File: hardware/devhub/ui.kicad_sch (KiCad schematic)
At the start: 12 parts, among them U10 74HC595, U11 74HC595

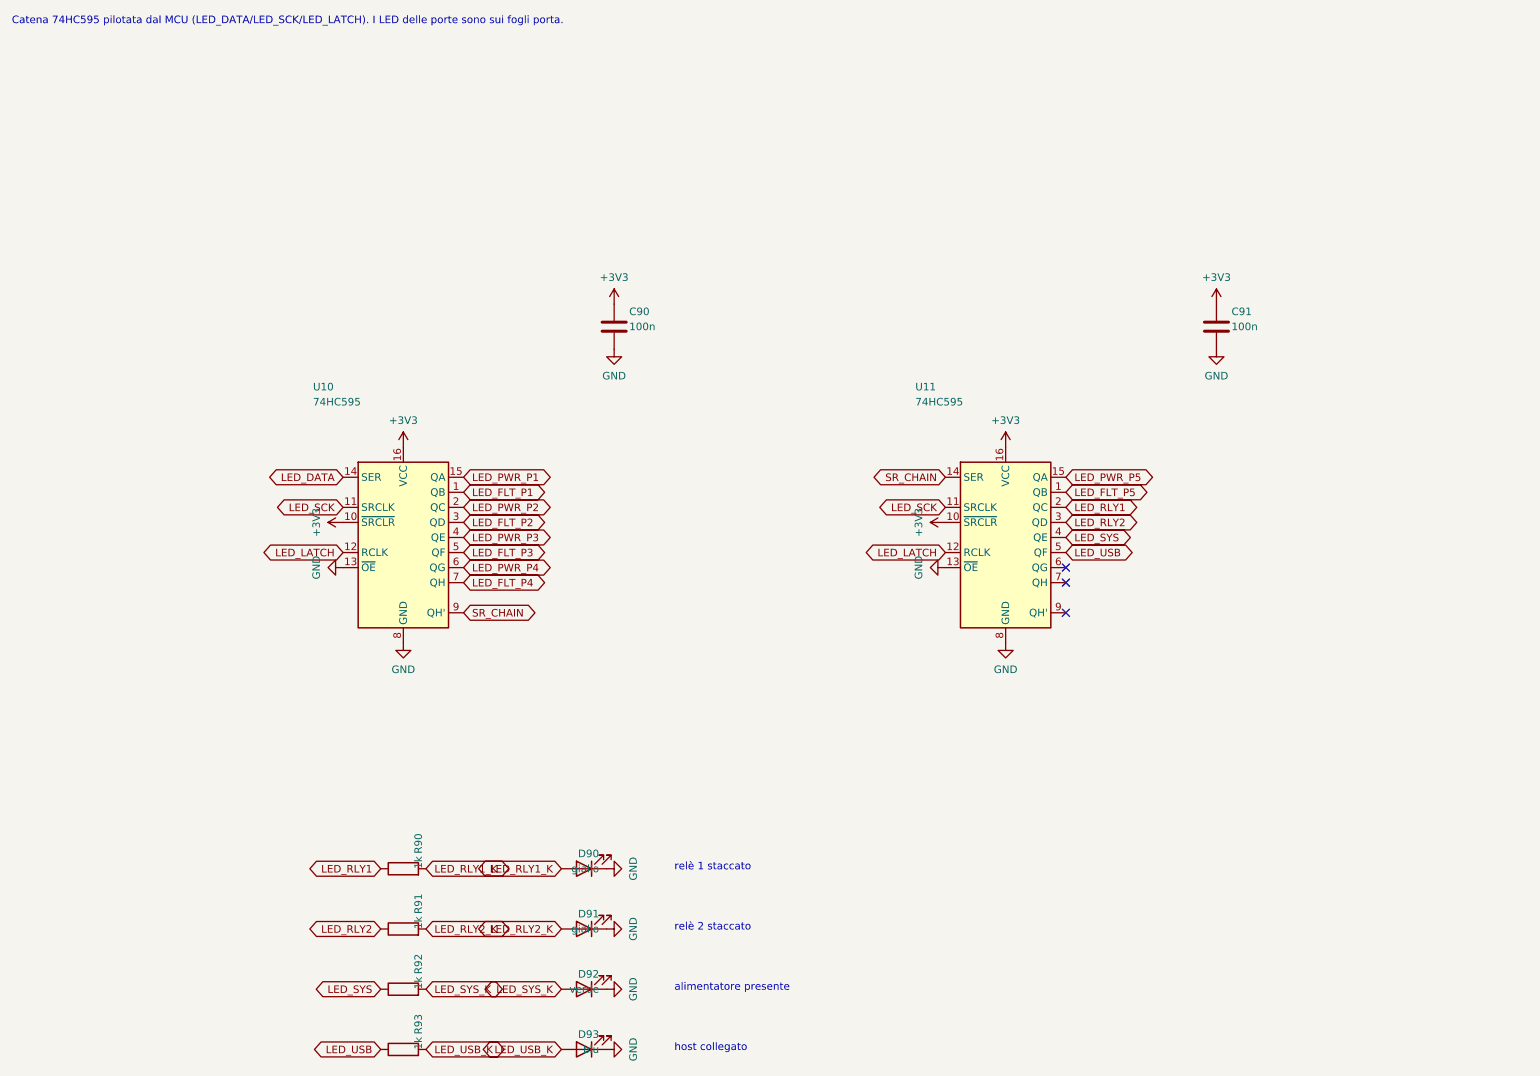
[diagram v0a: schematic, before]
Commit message: Schematic v0.2: hub reset supervisor, 1 A LDO, reorganized sheets, USB connectors and crystal
Functional changes:
- USB2517 RESET_N with pull-up and MCP120T-300 supervisor, wired-OR with
  the MCU (open-drain): resetting the MCU no longer resets the hub, so the
  ST DFU bootloader is reachable through it (D16/D17).
- 3.3 V LDO: AP7361C-33E (1 A, SOT-223) instead of AP2112K, which
  dissipated too much with the hub load.
- 74HC595 /OE on PB6 with pull-up: LEDs off until firmware enables them.
- Orange D93 instead of blue, USB-A bulk capacitance >= 120 uF, relay coil
  pinout fixed, snubbers marked DNP, Cliff FCR7350 banana jack footprints.
- D18: horizontal USB connectors, GCT USB4105-GF-A (USB-C) and Kycon
  KUSBX-AS1N-B (USB-A).
- D19: YXC X322524MOB4SI 24 MHz crystal (C_L 12 pF), 15 pF C0G load caps.

Layout: nearby parts wired directly, every net still explicitly named;
local labels inside sheets, global only across sheets, hierarchical for
ports. Files saved with KiCad 10.

Connectivity checked against the previous netlist, ERC clean.
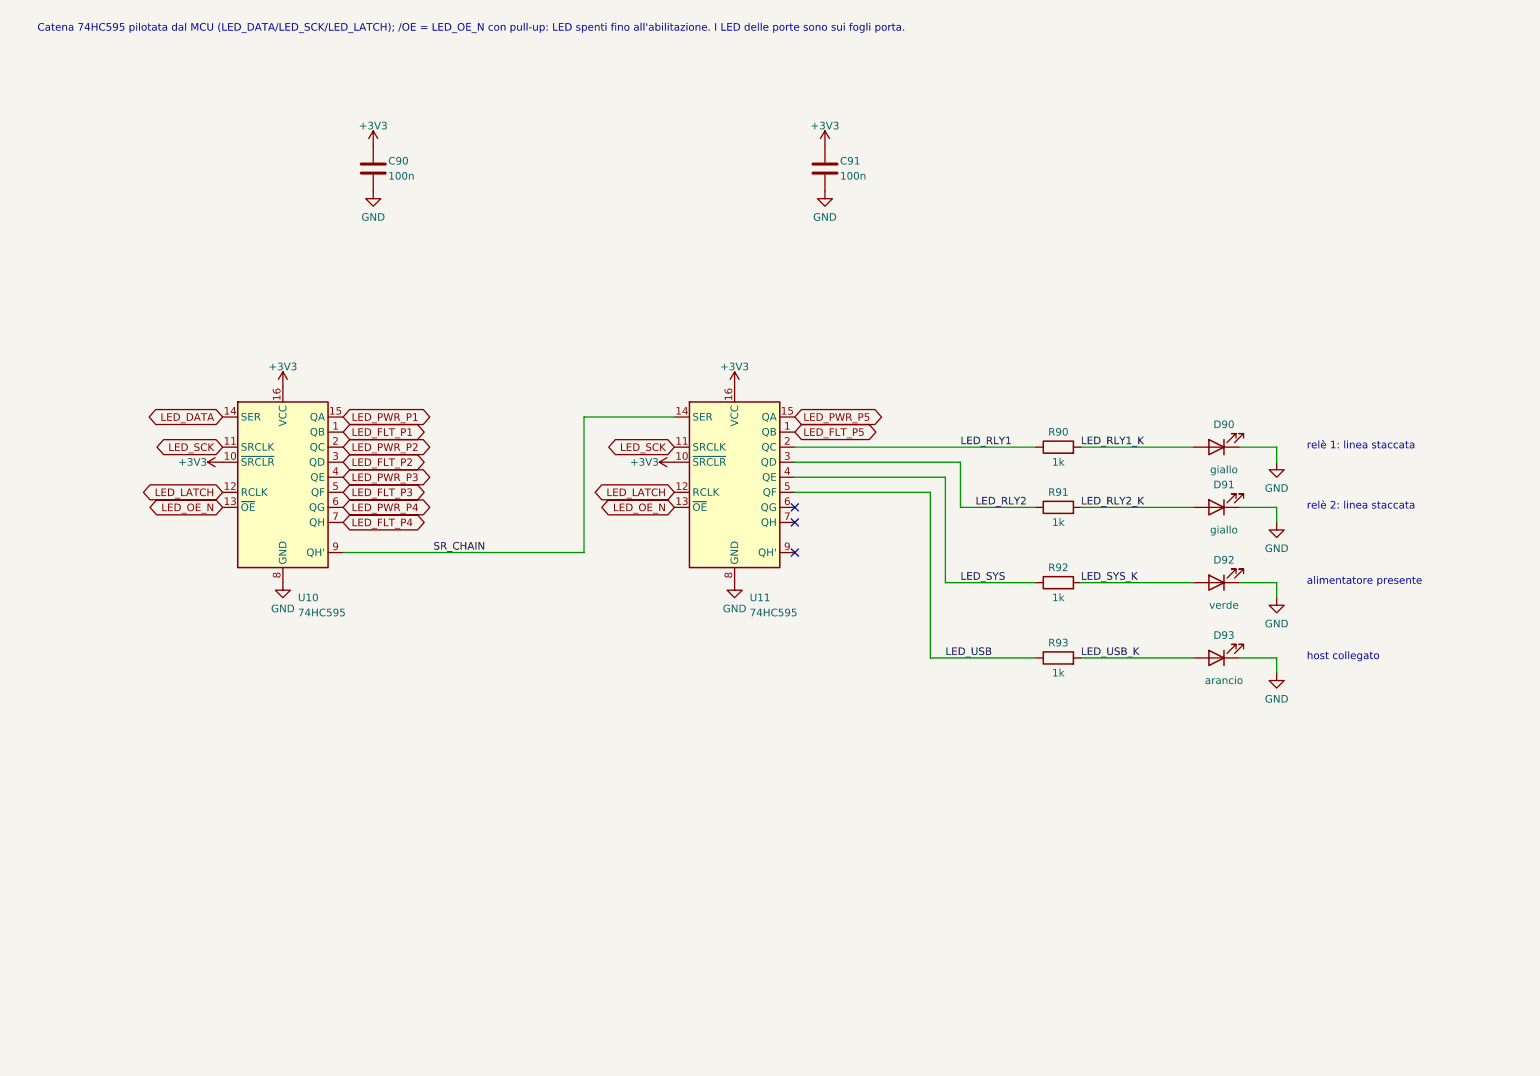
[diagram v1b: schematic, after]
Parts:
- D93: value blu -> arancio
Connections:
- net GND: no longer U10.13 (~{OE}), U11.13 (~{OE})
- new net LED_OE_N: U10.13 (~{OE}), U11.13 (~{OE})
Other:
- note added: "Catena 74HC595 pilotata dal MCU (LED_DATA/LED_SCK/LED_LATCH); /OE = LED_OE_N con pull-up: LED spenti fino all'abilitazione. I LED delle porte sono sui fogli porta."
- note added: "relè 1: linea staccata"
- note added: "relè 2: linea staccata"
- note removed: "Catena 74HC595 pilotata dal MCU (LED_DATA/LED_SCK/LED_LATCH). I LED delle porte sono sui fogli porta."
- note removed: "relè 1 staccato"
- note removed: "relè 2 staccato"

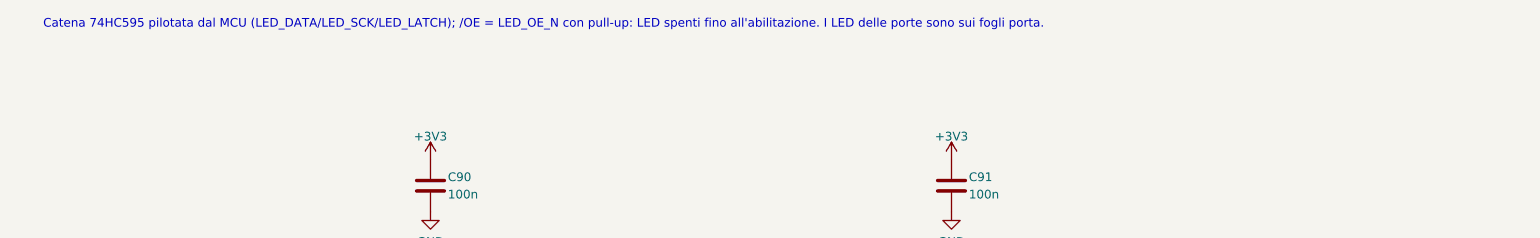
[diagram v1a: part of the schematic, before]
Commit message: Lab-use protection: TPS259470A input eFuse, PI3USB4002A data switches; AGENTS.md
Power input (D20, D21):
- TPS259470A eFuse after the shunt: trips above 5.84 V and below 4.0 V,
  zener on EN to withstand up to 28 V, 3.5 A limit, ~5 ms soft start,
  auto-retry, FLT to the MCU on PB1.
- The shunt stays before the eFuse, so the INA3221 still measures the input
  voltage when the eFuse is off.

Ports (D22): PI3USB4002A instead of TS3USB30E. The connector side withstands
24 V and opens above 4.75 V, so a D+/D- short to VBUS on a board under test
no longer reaches the 3.3 V rail.

Symbols for both ICs added to the project library. AGENTS.md added: the
schematic is edited in KiCad or with targeted changes, never regenerated by
script. Sheets re-saved by KiCad.

Connectivity checked against the previous netlist, ERC clean.
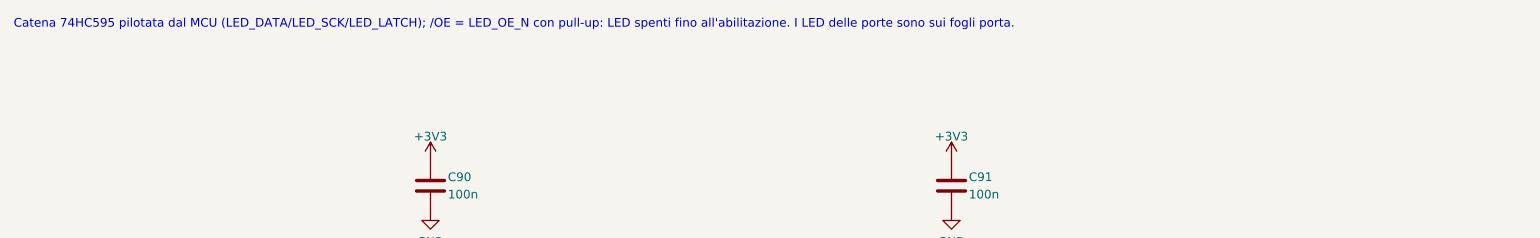
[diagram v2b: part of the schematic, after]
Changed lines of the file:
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@@
 	(text "Catena 74HC595 pilotata dal MCU (LED_DATA/LED_SCK/LED_LATCH); /OE = LED_OE_N con pull-up: LED spenti fino all'abilitazione. I LED delle porte sono sui fogli porta."
 		(exclude_from_sim no)
-		(at 14.478 16.51 0)
+		(at 10.16 16.51 0)
 		(effects
 			(font
@@
 		(in_pos_files yes)
 		(dnp no)
-		(property "Reference" "#PWR138"
+		(property "Reference" "#PWR145"
 			(at 71.12 35.56 0)
 			(hide yes)
@@
 			(project "devhub"
 				(path "/af6ea7d8-d1ba-5fc6-aec8-abf514847630/c82dde94-3a77-5cb6-9c61-f280daabce7c"
-					(reference "#PWR138")
+					(reference "#PWR145")
 					(unit 1)
 				)
@@
 		(in_pos_files yes)
 		(dnp no)
-		(property "Reference" "#PWR137"
+		(property "Reference" "#PWR144"
 			(at 132.08 76.2 0)
 			(hide yes)
@@
 			(project "devhub"
 				(path "/af6ea7d8-d1ba-5fc6-aec8-abf514847630/c82dde94-3a77-5cb6-9c61-f280daabce7c"
-					(reference "#PWR137")
+					(reference "#PWR144")
 					(unit 1)
 				)
@@
 		(in_pos_files yes)
 		(dnp no)
-		(property "Reference" "#PWR140"
+		(property "Reference" "#PWR147"
 			(at 147.32 35.56 0)
 			(hide yes)
@@
 			(project "devhub"
 				(path "/af6ea7d8-d1ba-5fc6-aec8-abf514847630/c82dde94-3a77-5cb6-9c61-f280daabce7c"
-					(reference "#PWR140")
+					(reference "#PWR147")
 					(unit 1)
 				)
@@
 		(in_pos_files yes)
 		(dnp no)
-		(property "Reference" "#PWR133"
+		(property "Reference" "#PWR140"
 			(at 45.72 88.9 0)
 			(hide yes)
@@
 			(project "devhub"
 				(path "/af6ea7d8-d1ba-5fc6-aec8-abf514847630/c82dde94-3a77-5cb6-9c61-f280daabce7c"
-					(reference "#PWR133")
+					(reference "#PWR140")
 					(unit 1)
 				)
@@
 		(in_pos_files yes)
 		(dnp no)
-		(property "Reference" "#PWR136"
+		(property "Reference" "#PWR143"
 			(at 121.92 88.9 0)
 			(hide yes)
@@
 			(project "devhub"
 				(path "/af6ea7d8-d1ba-5fc6-aec8-abf514847630/c82dde94-3a77-5cb6-9c61-f280daabce7c"
-					(reference "#PWR136")
+					(reference "#PWR143")
 					(unit 1)
 				)
@@
 		(in_pos_files yes)
 		(dnp no)
-		(property "Reference" "#PWR134"
+		(property "Reference" "#PWR141"
 			(at 55.88 76.2 0)
 			(hide yes)
@@
 			(project "devhub"
 				(path "/af6ea7d8-d1ba-5fc6-aec8-abf514847630/c82dde94-3a77-5cb6-9c61-f280daabce7c"
-					(reference "#PWR134")
+					(reference "#PWR141")
 					(unit 1)
 				)
@@
 		(in_pos_files yes)
 		(dnp no)
-		(property "Reference" "#PWR139"
+		(property "Reference" "#PWR146"
 			(at 71.12 43.18 0)
 			(hide yes)
@@
 			(project "devhub"
 				(path "/af6ea7d8-d1ba-5fc6-aec8-abf514847630/c82dde94-3a77-5cb6-9c61-f280daabce7c"
-					(reference "#PWR139")
+					(reference "#PWR146")
 					(unit 1)
 				)
@@
 		(in_pos_files yes)
 		(dnp no)
-		(property "Reference" "#PWR141"
+		(property "Reference" "#PWR148"
 			(at 147.32 43.18 0)
 			(hide yes)
@@
 			(project "devhub"
 				(path "/af6ea7d8-d1ba-5fc6-aec8-abf514847630/c82dde94-3a77-5cb6-9c61-f280daabce7c"
-					(reference "#PWR141")
+					(reference "#PWR148")
 					(unit 1)
 				)
@@
 		(in_pos_files yes)
 		(dnp no)
-		(property "Reference" "#PWR145"
+		(property "Reference" "#PWR152"
 			(at 223.52 124.46 0)
 			(hide yes)
@@
 			(project "devhub"
 				(path "/af6ea7d8-d1ba-5fc6-aec8-abf514847630/c82dde94-3a77-5cb6-9c61-f280daabce7c"
-					(reference "#PWR145")
+					(reference "#PWR152")
 					(unit 1)
 				)
@@
 		(in_pos_files yes)
 		(dnp no)
-		(property "Reference" "#PWR144"
+		(property "Reference" "#PWR151"
 			(at 223.52 111.76 0)
 			(hide yes)
@@
 			(project "devhub"
 				(path "/af6ea7d8-d1ba-5fc6-aec8-abf514847630/c82dde94-3a77-5cb6-9c61-f280daabce7c"
-					(reference "#PWR144")
+					(reference "#PWR151")
 					(unit 1)
 				)
@@
 		(in_pos_files yes)
 		(dnp no)
-		(property "Reference" "#PWR135"
+		(property "Reference" "#PWR142"
 			(at 132.08 109.22 0)
 			(hide yes)
@@
 			(project "devhub"
 				(path "/af6ea7d8-d1ba-5fc6-aec8-abf514847630/c82dde94-3a77-5cb6-9c61-f280daabce7c"
-					(reference "#PWR135")
+					(reference "#PWR142")
 					(unit 1)
 				)
@@
 		(in_pos_files yes)
 		(dnp no)
-		(property "Reference" "#PWR132"
+		(property "Reference" "#PWR139"
 			(at 55.88 109.22 0)
 			(hide yes)
@@
 			(project "devhub"
 				(path "/af6ea7d8-d1ba-5fc6-aec8-abf514847630/c82dde94-3a77-5cb6-9c61-f280daabce7c"
-					(reference "#PWR132")
+					(reference "#PWR139")
 					(unit 1)
 				)
@@
 		(in_pos_files yes)
 		(dnp no)
-		(property "Reference" "#PWR142"
+		(property "Reference" "#PWR149"
 			(at 223.52 88.9 0)
 			(hide yes)
@@
 			(project "devhub"
 				(path "/af6ea7d8-d1ba-5fc6-aec8-abf514847630/c82dde94-3a77-5cb6-9c61-f280daabce7c"
-					(reference "#PWR142")
+					(reference "#PWR149")
 					(unit 1)
 				)
@@
 		(in_pos_files yes)
 		(dnp no)
-		(property "Reference" "#PWR143"
+		(property "Reference" "#PWR150"
 			(at 223.52 99.06 0)
 			(hide yes)
@@
 			(project "devhub"
 				(path "/af6ea7d8-d1ba-5fc6-aec8-abf514847630/c82dde94-3a77-5cb6-9c61-f280daabce7c"
-					(reference "#PWR143")
+					(reference "#PWR150")
 					(unit 1)
 				)

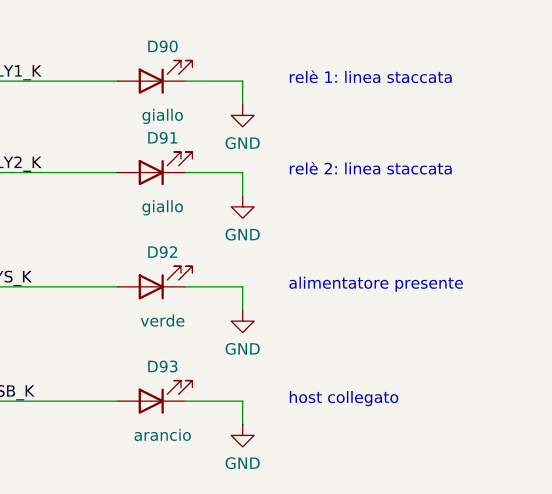
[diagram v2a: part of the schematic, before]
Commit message: Review 02, R02-05: drop RF-16, logic powered from the supply only (D32)
Removed D3; VBUS_DET and VSYS_ADC moved to 5 V tolerant pins (PA6, PA7).
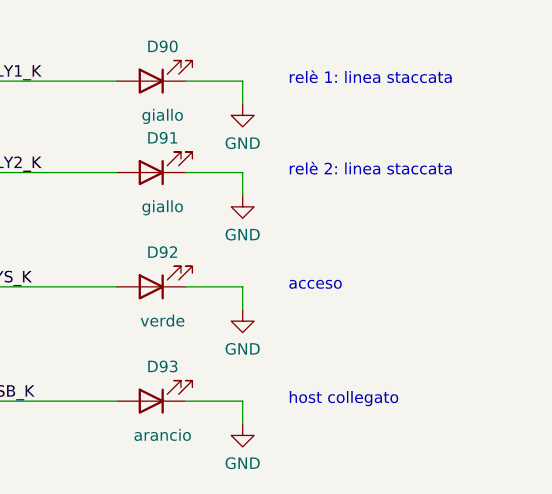
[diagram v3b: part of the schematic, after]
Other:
- note added: "acceso"
- note removed: "alimentatore presente"
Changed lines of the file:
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@@
 		)
 	)
-	(text "alimentatore presente"
+	(text "acceso"
 		(exclude_from_sim no)
 		(at 228.6 109.82 0)
